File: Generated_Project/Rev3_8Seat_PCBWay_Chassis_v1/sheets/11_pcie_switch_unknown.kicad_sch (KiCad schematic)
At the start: 0 parts

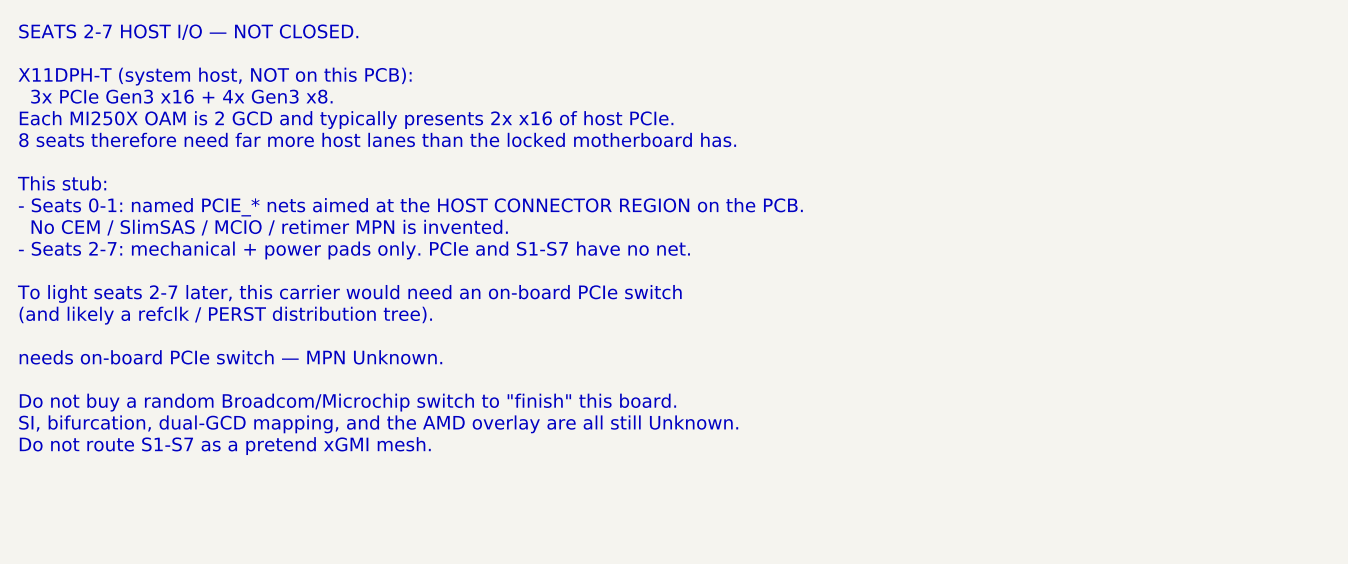
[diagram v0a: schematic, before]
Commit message: Raise Rev3 chassis to 8 electrically designed seats.
Name v1.0 power/PE/clock nets on all eight OAM seats toward two DNP
PM8536B-FEI (x8 per GCD), keep SB175 star + local P48V pours, and generate
the 12-layer 2.0 mm stuffed-switch target. First stuffing may still populate
two modules; the PCB does not need a respin for the other six.

Do not fabricate. Do not energize P48V.

Co-authored-by: zivzancoeli-commits <zivzancoeli-commits@users.noreply.github.com>
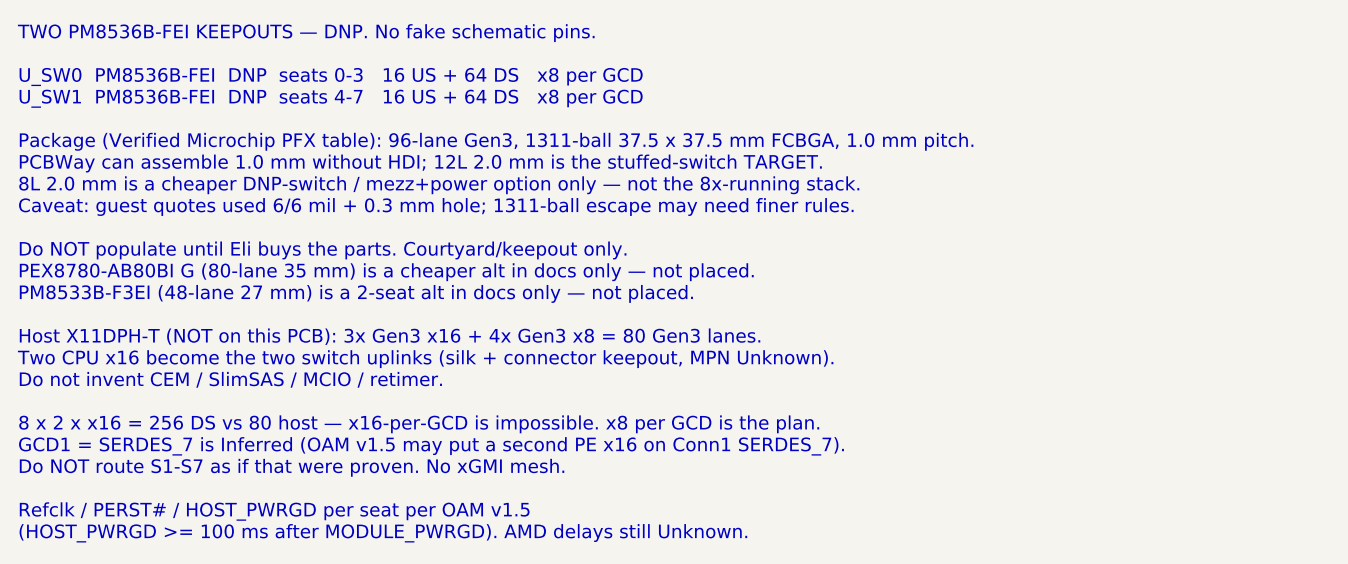
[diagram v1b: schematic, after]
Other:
- note added: "TWO PM8536B-FEI KEEPOUTS — DNP. No fake schematic pins. U_SW0 PM8536B-FEI DNP seats 0-3 16 US + 64 DS x8 per GCD U_SW1 PM8536B-FEI DNP seats 4-7 16 US + 64 DS x8 per GCD Package (Verified Microchip PFX table): 96-lane Gen3, 1311-ball 37.5 x 37.5 mm FCBGA, 1.0 mm pitch. PCBWay can assemble 1.0 mm without HDI; 12L 2.0 mm is the stuffed-switch TARGET. 8L 2.0 mm is a cheaper DNP-switch / mezz+power o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"
- note removed: "SEATS 2-7 HOST I/O — NOT CLOSED. X11DPH-T (system host, NOT on this PCB): 3x PCIe Gen3 x16 + 4x Gen3 x8. Each MI250X OAM is 2 GCD and typically presents 2x x16 of host PCIe. 8 seats therefore need far more host lanes than the locked motherboard has. This stub: - Seats 0-1: named PCIE_* nets aimed at the HOST CONNECTOR REGION on the PCB. No CEM / SlimSAS / MCIO / retimer MPN is invented. - Seats 2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"
- title: PCIe switch MPN Unknown -> PM8536B-FEI DNP x2 (keepout only)
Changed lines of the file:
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@@
 	(paper "A3")
 	(title_block
-		(title "PCIe switch MPN Unknown")
+		(title "PM8536B-FEI DNP x2 (keepout only)")
 		(date "2026-08-21")
 		(rev "Rev3_8Seat_PCBWay_v1")
-		(comment 1 "DO NOT FABRICATE. DO NOT ENERGIZE P48V. Ticket 167157 open.")
-		(comment 2 "Documentation sheet — no invented nets")
-		(comment 3 "Pin names: OAM Pin map rev 1.0.xlsx — OCP generic, NOT AMD overlay")
-		(comment 4 "r2.0 maps UNUSABLE. P3V3=2 Conn0 C1/C2. 8-seat PCBWay chassis stub.")
+        (comment 1 "DO NOT FABRICATE. DO NOT ENERGIZE P48V. Molex 60V written 2026-08-18; 1.2A/contact OPEN.")
+        (comment 2 "Documentation sheet — no invented nets")
+        (comment 3 "Pin names: OAM Pin map rev 1.0.xlsx — OCP generic, NOT AMD overlay")
+        (comment 4 "r2.0 UNUSABLE. P3V3=Conn0 C1/C2. 12L 2.0mm stuffed-switch TARGET. Star-fed P48V.")
 	)
-	(text "SEATS 2-7 HOST I/O — NOT CLOSED.\n\nX11DPH-T (system host, NOT on this PCB):\n  3x PCIe Gen3 x16 + 4x Gen3 x8.\nEach MI250X OAM is 2 GCD and typically presents 2x x16 of host PCIe.\n8 seats therefore need far more host lanes than the locked motherboard has.\n\nThis stub:\n- Seats 0-1: named PCIE_* nets aimed at the HOST CONNECTOR REGION on the PCB.\n  No CEM / SlimSAS / MCIO / retimer MPN is invented.\n- Seats 2-7: mechanical + power pads only. PCIe and S1-S7 have no net.\n\nTo light seats 2-7 later, this carrier would need an on-board PCIe switch\n(and likely a refclk / PERST distribution tree).\n\nneeds on-board PCIe switch — MPN Unknown.\n\nDo not buy a random Broadcom/Microchip switch to \"finish\" this board.\nSI, bifurcation, dual-GCD mapping, and the AMD overlay are all still Unknown.\nDo not route S1-S7 as a pretend xGMI mesh.\n"
+	(text "TWO PM8536B-FEI KEEPOUTS — DNP. No fake schematic pins.\n\nU_SW0  PM8536B-FEI  DNP  seats 0-3   16 US + 64 DS   x8 per GCD\nU_SW1  PM8536B-FEI  DNP  seats 4-7   16 US + 64 DS   x8 per GCD\n\nPackage (Verified Microchip PFX table): 96-lane Gen3, 1311-ball 37.5 x 37.5 mm FCBGA, 1.0 mm pitch.\nPCBWay can assemble 1.0 mm without HDI; 12L 2.0 mm is the stuffed-switch TARGET.\n8L 2.0 mm is a cheaper DNP-switch / mezz+power option only — not the 8x-running stack.\nCaveat: guest quotes used 6/6 mil + 0.3 mm hole; 1311-ball escape may need finer rules.\n\nDo NOT populate until Eli buys the parts. Courtyard/keepout only.\nPEX8780-AB80BI G (80-lane 35 mm) is a cheaper alt in docs only — not placed.\nPM8533B-F3EI (48-lane 27 mm) is a 2-seat alt in docs only — not placed.\n\nHost X11DPH-T (NOT on this PCB): 3x Gen3 x16 + 4x Gen3 x8 = 80 Gen3 lanes.\nTwo CPU x16 become the two switch uplinks (silk + connector keepout, MPN Unknown).\nDo not invent CEM / SlimSAS / MCIO / retimer.\n\n8 x 2 x x16 = 256 DS vs 80 host — x16-per-GCD is impossible. x8 per GCD is the plan.\nGCD1 = SERDES_7 is Inferred (OAM v1.5 may put a second PE x16 on Conn1 SERDES_7).\nDo NOT route S1-S7 as if that were proven. No xGMI mesh.\n\nRefclk / PERST# / HOST_PWRGD per seat per OAM v1.5\n(HOST_PWRGD >= 100 ms after MODULE_PWRGD). AMD delays still Unknown.\n"
 		(exclude_from_sim no)
 		(at 20.32 20.32 0)

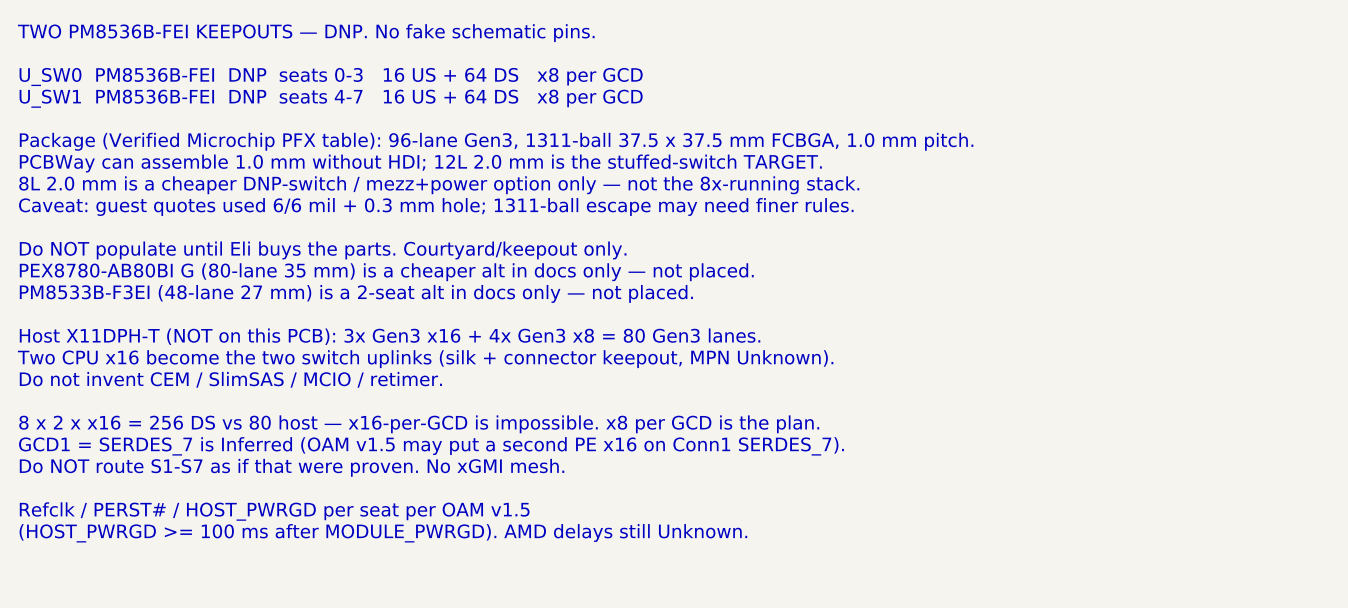
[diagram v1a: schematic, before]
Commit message: Label PEX8780-AB80BI G as the only switch CANDIDATE (DNP).
Keepout is one 35 mm 1156-FCBGA for 8x x8 Gen3 plus one x16 host uplink.
Do not invent a second MPN. Do not stuff. 8-layer is likely if this BGA
is ever assembled; PCBWay 1156-FCBGA attach remains Unknown.

Still do not fabricate or energize P48V. No xGMI, no CEM.

Co-authored-by: zivzancoeli-commits <zivzancoeli-commits@users.noreply.github.com>
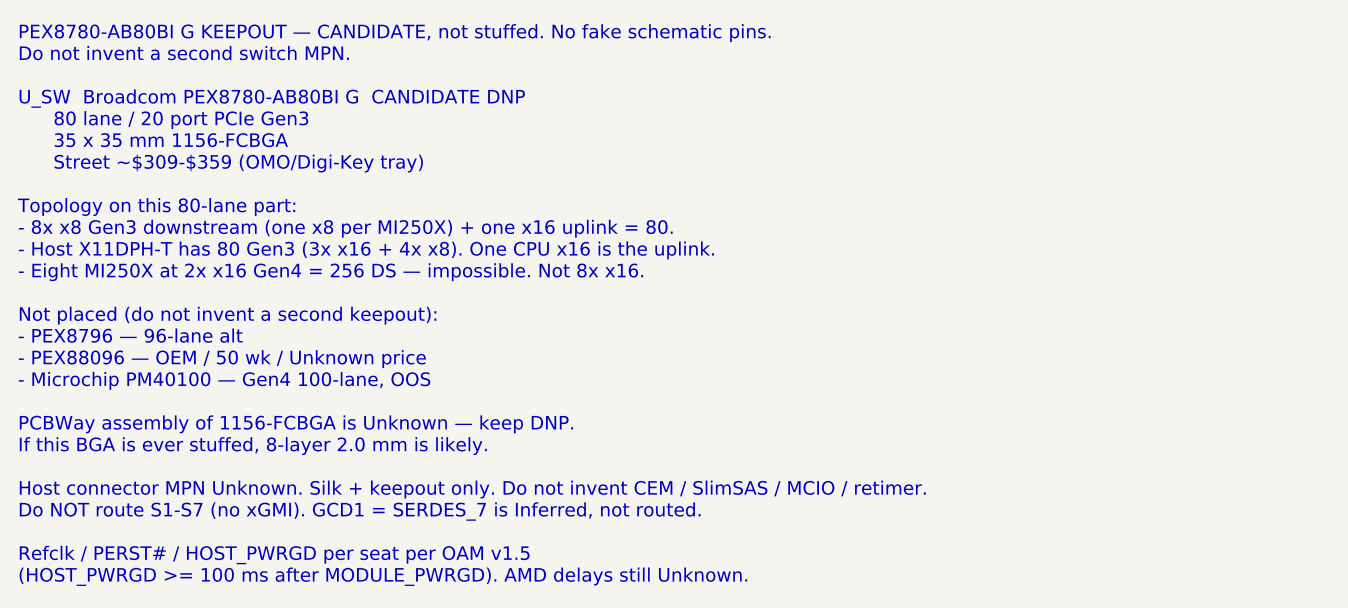
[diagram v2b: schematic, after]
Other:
- note added: "PEX8780-AB80BI G KEEPOUT — CANDIDATE, not stuffed. No fake schematic pins. Do not invent a second switch MPN. U_SW Broadcom PEX8780-AB80BI G CANDIDATE DNP 80 lane / 20 port PCIe Gen3 35 x 35 mm 1156-FCBGA Street ~$309-$359 (OMO/Digi-Key tray) Topology on this 80-lane part: - 8x x8 Gen3 downstream (one x8 per MI250X) + one x16 uplink = 80. - Host X11DPH-T has 80 Gen3 (3x x16 + 4x x8). One CPU x16 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"
- note removed: "TWO PM8536B-FEI KEEPOUTS — DNP. No fake schematic pins. U_SW0 PM8536B-FEI DNP seats 0-3 16 US + 64 DS x8 per GCD U_SW1 PM8536B-FEI DNP seats 4-7 16 US + 64 DS x8 per GCD Package (Verified Microchip PFX table): 96-lane Gen3, 1311-ball 37.5 x 37.5 mm FCBGA, 1.0 mm pitch. PCBWay can assemble 1.0 mm without HDI; 12L 2.0 mm is the stuffed-switch TARGET. 8L 2.0 mm is a cheaper DNP-switch / mezz+power o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"
- title: PM8536B-FEI DNP x2 (keepout only) -> PEX8780-AB80BI G CANDIDATE (keepout, not stuffed)
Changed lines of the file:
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@@
 	(paper "A3")
 	(title_block
-		(title "PM8536B-FEI DNP x2 (keepout only)")
+		(title "PEX8780-AB80BI G CANDIDATE (keepout, not stuffed)")
 		(date "2026-08-21")
 		(rev "Rev3_8Seat_PCBWay_v1")
@@
         (comment 4 "r2.0 UNUSABLE. P3V3=Conn0 C1/C2. 12L 2.0mm stuffed-switch TARGET. Star-fed P48V.")
 	)
-	(text "TWO PM8536B-FEI KEEPOUTS — DNP. No fake schematic pins.\n\nU_SW0  PM8536B-FEI  DNP  seats 0-3   16 US + 64 DS   x8 per GCD\nU_SW1  PM8536B-FEI  DNP  seats 4-7   16 US + 64 DS   x8 per GCD\n\nPackage (Verified Microchip PFX table): 96-lane Gen3, 1311-ball 37.5 x 37.5 mm FCBGA, 1.0 mm pitch.\nPCBWay can assemble 1.0 mm without HDI; 12L 2.0 mm is the stuffed-switch TARGET.\n8L 2.0 mm is a cheaper DNP-switch / mezz+power option only — not the 8x-running stack.\nCaveat: guest quotes used 6/6 mil + 0.3 mm hole; 1311-ball escape may need finer rules.\n\nDo NOT populate until Eli buys the parts. Courtyard/keepout only.\nPEX8780-AB80BI G (80-lane 35 mm) is a cheaper alt in docs only — not placed.\nPM8533B-F3EI (48-lane 27 mm) is a 2-seat alt in docs only — not placed.\n\nHost X11DPH-T (NOT on this PCB): 3x Gen3 x16 + 4x Gen3 x8 = 80 Gen3 lanes.\nTwo CPU x16 become the two switch uplinks (silk + connector keepout, MPN Unknown).\nDo not invent CEM / SlimSAS / MCIO / retimer.\n\n8 x 2 x x16 = 256 DS vs 80 host — x16-per-GCD is impossible. x8 per GCD is the plan.\nGCD1 = SERDES_7 is Inferred (OAM v1.5 may put a second PE x16 on Conn1 SERDES_7).\nDo NOT route S1-S7 as if that were proven. No xGMI mesh.\n\nRefclk / PERST# / HOST_PWRGD per seat per OAM v1.5\n(HOST_PWRGD >= 100 ms after MODULE_PWRGD). AMD delays still Unknown.\n"
+	(text "PEX8780-AB80BI G KEEPOUT — CANDIDATE, not stuffed. No fake schematic pins.\nDo not invent a second switch MPN.\n\nU_SW  Broadcom PEX8780-AB80BI G  CANDIDATE DNP\n      80 lane / 20 port PCIe Gen3\n      35 x 35 mm 1156-FCBGA\n      Street ~$309-$359 (OMO/Digi-Key tray)\n\nTopology on this 80-lane part:\n- 8x x8 Gen3 downstream (one x8 per MI250X) + one x16 uplink = 80.\n- Host X11DPH-T has 80 Gen3 (3x x16 + 4x x8). One CPU x16 is the uplink.\n- Eight MI250X at 2x x16 Gen4 = 256 DS — impossible. Not 8x x16.\n\nNot placed (do not invent a second keepout):\n- PEX8796 — 96-lane alt\n- PEX88096 — OEM / 50 wk / Unknown price\n- Microchip PM40100 — Gen4 100-lane, OOS\n\nPCBWay assembly of 1156-FCBGA is Unknown — keep DNP.\nIf this BGA is ever stuffed, 8-layer 2.0 mm is likely.\n\nHost connector MPN Unknown. Silk + keepout only. Do not invent CEM / SlimSAS / MCIO / retimer.\nDo NOT route S1-S7 (no xGMI). GCD1 = SERDES_7 is Inferred, not routed.\n\nRefclk / PERST# / HOST_PWRGD per seat per OAM v1.5\n(HOST_PWRGD >= 100 ms after MODULE_PWRGD). AMD delays still Unknown.\n"
 		(exclude_from_sim no)
 		(at 20.32 20.32 0)
